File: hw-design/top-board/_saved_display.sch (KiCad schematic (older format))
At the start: 32 parts, among them P5 BACKLIGHT, P6 BACKLIGHT, Q2 MMBT2222A, Q3 MMBT2222A

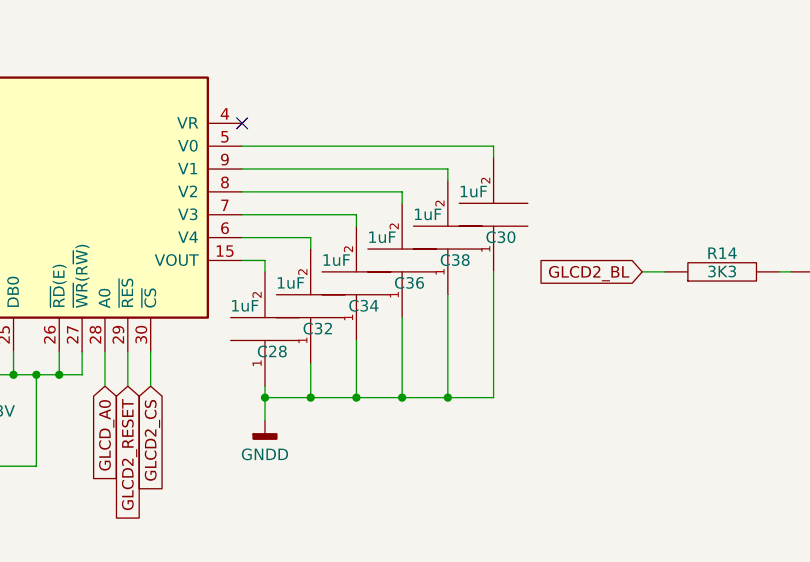
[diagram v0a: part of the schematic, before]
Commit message: Fixed ERC & DRC tests
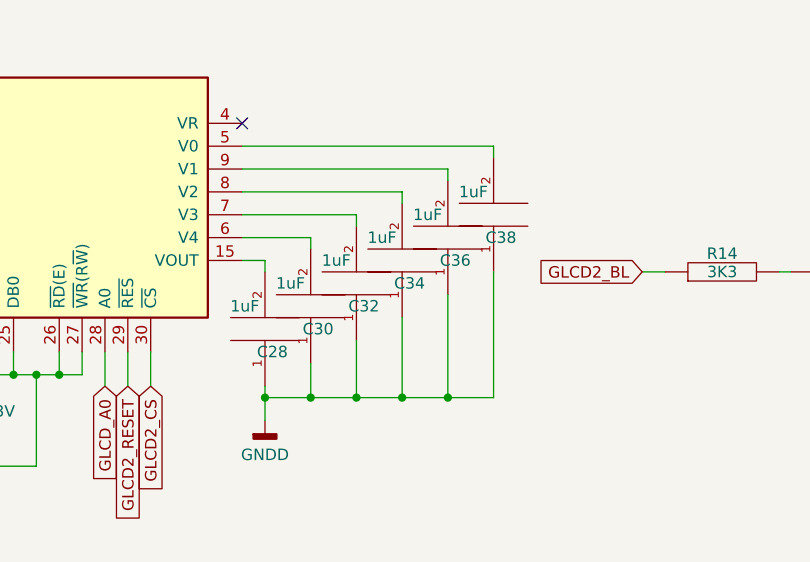
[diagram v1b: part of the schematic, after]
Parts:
- renumbered C32 to C30, C34 to C32, C36 to C34, C38 to C36, C30 to C38
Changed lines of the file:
@@
 $EndComp
 $Comp
-L C C32
+L C C30
 U 1 1 5554DE6B
 P 6800 4800
-F 0 "C32" H 6700 4900 50  0000 L CNN
+F 0 "C30" H 6700 4900 50  0000 L CNN
 F 1 "1uF" H 6825 4700 50  0000 L CNN
 F 2 "Capacitors_SMD:C_0805" H 6838 4650 30  0001 C CNN
@@
 $EndComp
 $Comp
-L C C34
+L C C32
 U 1 1 5554DE71
 P 7000 4700
-F 0 "C34" H 6900 4800 50  0000 L CNN
+F 0 "C32" H 6900 4800 50  0000 L CNN
 F 1 "1uF" H 7025 4600 50  0000 L CNN
 F 2 "Capacitors_SMD:C_0805" H 7038 4550 30  0001 C CNN
@@
 $EndComp
 $Comp
-L C C36
+L C C34
 U 1 1 5554DE77
 P 7200 4600
-F 0 "C36" H 7100 4700 50  0000 L CNN
+F 0 "C34" H 7100 4700 50  0000 L CNN
 F 1 "1uF" H 7225 4500 50  0000 L CNN
 F 2 "Capacitors_SMD:C_0805" H 7238 4450 30  0001 C CNN
@@
 $EndComp
 $Comp
-L C C38
+L C C36
 U 1 1 5554DE7D
 P 7400 4500
-F 0 "C38" H 7300 4600 50  0000 L CNN
+F 0 "C36" H 7300 4600 50  0000 L CNN
 F 1 "1uF" H 7425 4400 50  0000 L CNN
 F 2 "Capacitors_SMD:C_0805" H 7438 4350 30  0001 C CNN
@@
 	6500 4500 6800 4500
 $Comp
-L C C30
+L C C38
 U 1 1 5AFE90D7
 P 7600 4400
-F 0 "C30" H 7500 4500 50  0000 L CNN
+F 0 "C38" H 7500 4500 50  0000 L CNN
 F 1 "1uF" H 7625 4300 50  0000 L CNN
 F 2 "Capacitors_SMD:C_0805" H 7638 4250 30  0001 C CNN
